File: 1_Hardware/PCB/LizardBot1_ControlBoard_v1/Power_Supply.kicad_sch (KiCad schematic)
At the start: 49 parts, among them J201 Conn_01x02, J202 Screw_Terminal_01x02, J203 Conn_01x02, J204 Conn_01x02, J205 Conn_01x02, Q201 SQ4425EY, Q202 AO3401A, SW201 SW_SPST, SW202 SW_Push, U202 AP2112K-3.3

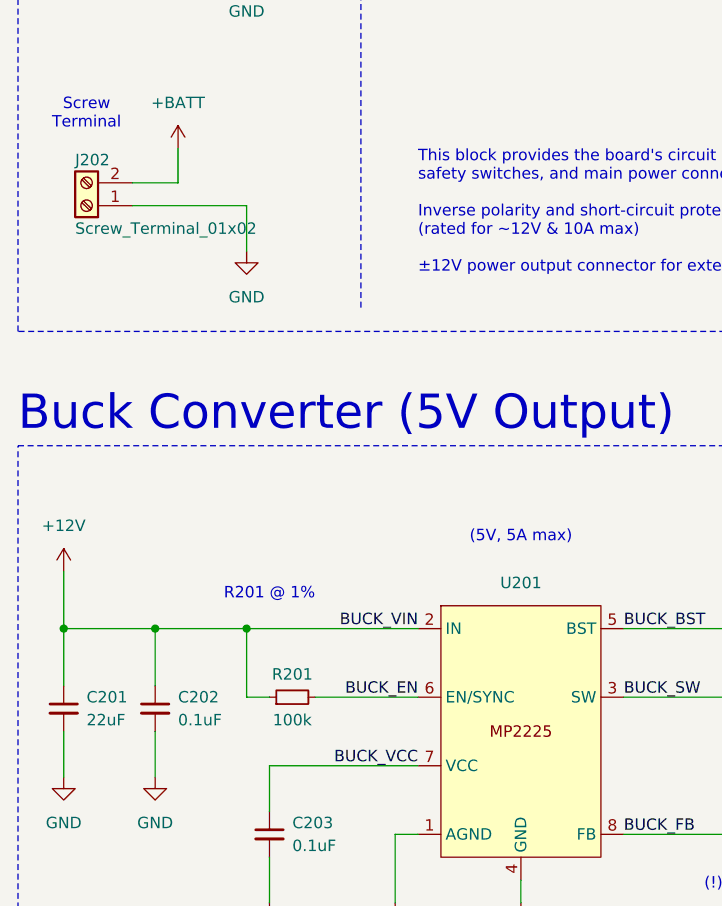
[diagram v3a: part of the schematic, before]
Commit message: Added Peripherals schematic
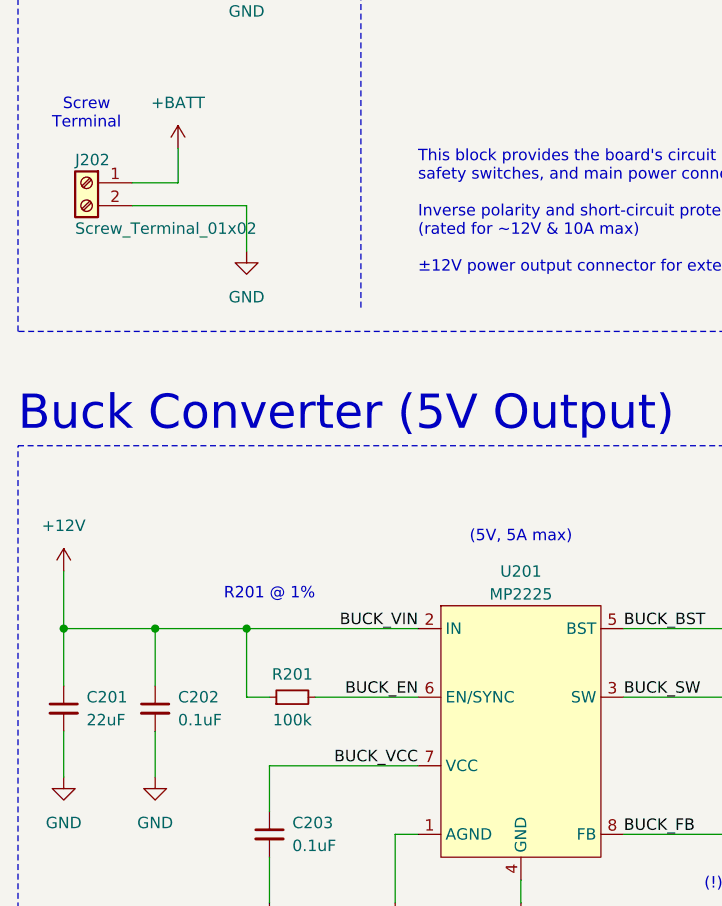
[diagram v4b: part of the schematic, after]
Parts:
- U201: value ~ -> MP2225
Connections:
- net +BATT: now also J202.1 (Pin_1); no longer J202.2 (Pin_2)
- net GND: now also J202.2 (Pin_2); no longer J202.1 (Pin_1)
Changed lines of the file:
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@@
+	)
+	(symbol
+		(lib_id "Connector:Screw_Terminal_01x02")
+		(at 26.67 77.47 0)
+		(mirror y)
+		(unit 1)
+		(exclude_from_sim no)
+		(in_bom yes)
+		(on_board yes)
+		(dnp no)
+		(property "Reference" "J202"
+			(at 25.4 74.93 0)
+			(effects
+				(font
+					(size 1.27 1.27)
+				)
+				(justify right)
+			)
+		)
+		(property "Value" "Screw_Terminal_01x02"
+			(at 25.4 82.55 0)
+			(effects
+				(font
+					(size 1.27 1.27)
+				)
+				(justify right)
+			)
+		)
+		(property "Footprint" ""
+			(at 26.67 77.47 0)
+			(effects
+				(font
+					(size 1.27 1.27)
+				)
+				(hide yes)
+			)
+		)
+		(property "Datasheet" "~"
+			(at 26.67 77.47 0)
+			(effects
+				(font
+					(size 1.27 1.27)
+				)
+				(hide yes)
+			)
+		)
+		(property "Description" "Generic screw terminal, single row, 01x02, script generated (kicad-library-utils/schlib/autogen/connector/)"
+			(at 26.67 77.47 0)
+			(effects
+				(font
+					(size 1.27 1.27)
+				)
+				(hide yes)
+			)
+		)
+		(pin "1"
+		)
+		(pin "2"
+		)
+		(instances
+			(project "LizardBot1_ControlBoard_v1"
+				(path "/1a674a4d-d877-4d7a-ad57-e0a054705c31/1ad8e535-9964-46ac-bb04-941393eb127d"
+					(reference "J202")
+					(unit 1)
+				)
+			)
+		)
 	)
 	(symbol
@@
 		(on_board yes)
 		(dnp no)
-		(fields_autoplaced yes)
 		(property "Reference" "U201"
-			(at 74.93 121.92 0)
-			(effects
-				(font
-					(size 1.27 1.27)
-				)
-			)
-		)
-		(property "Value" "~"
-			(at 74.93 138.43 0)
-			(effects
-				(font
-					(size 1.27 1.27)
-				)
-				(hide yes)
+			(at 74.93 120.65 0)
+			(effects
+				(font
+					(size 1.27 1.27)
+				)
+			)
+		)
+		(property "Value" "MP2225"
+			(at 74.93 123.19 0)
+			(effects
+				(font
+					(size 1.27 1.27)
+				)
 			)
 		)
@@
 					(unit 1)
 				)
-			)
-		)
-	)
-	(symbol
-		(lib_id "Connector:Screw_Terminal_01x02")
-		(at 26.67 80.01 180)
-		(unit 1)
-		(exclude_from_sim no)
-		(in_bom yes)
-		(on_board yes)
-		(dnp no)
-		(property "Reference" "J202"
-			(at 25.4 74.93 0)
-			(effects
-				(font
-					(size 1.27 1.27)
-				)
-				(justify right)
-			)
-		)
-		(property "Value" "Screw_Terminal_01x02"
-			(at 25.4 82.55 0)
-			(effects
-				(font
-					(size 1.27 1.27)
-				)
-				(justify right)
-			)
-		)
-		(property "Footprint" ""
-			(at 26.67 80.01 0)
-			(effects
-				(font
-					(size 1.27 1.27)
-				)
-				(hide yes)
-			)
-		)
-		(property "Datasheet" "~"
-			(at 26.67 80.01 0)
-			(effects
-				(font
-					(size 1.27 1.27)
-				)
-				(hide yes)
-			)
-		)
-		(property "Description" "Generic screw terminal, single row, 01x02, script generated (kicad-library-utils/schlib/autogen/connector/)"
-			(at 26.67 80.01 0)
-			(effects
-				(font
-					(size 1.27 1.27)
-				)
-				(hide yes)
-			)
-		)
-		(pin "1"
-		)
-		(pin "2"
-		)
-		(instances
-			(project ""
-				(path "/1a674a4d-d877-4d7a-ad57-e0a054705c31/1ad8e535-9964-46ac-bb04-941393eb127d"
-					(reference "J202")
-					(unit 1)
-				)

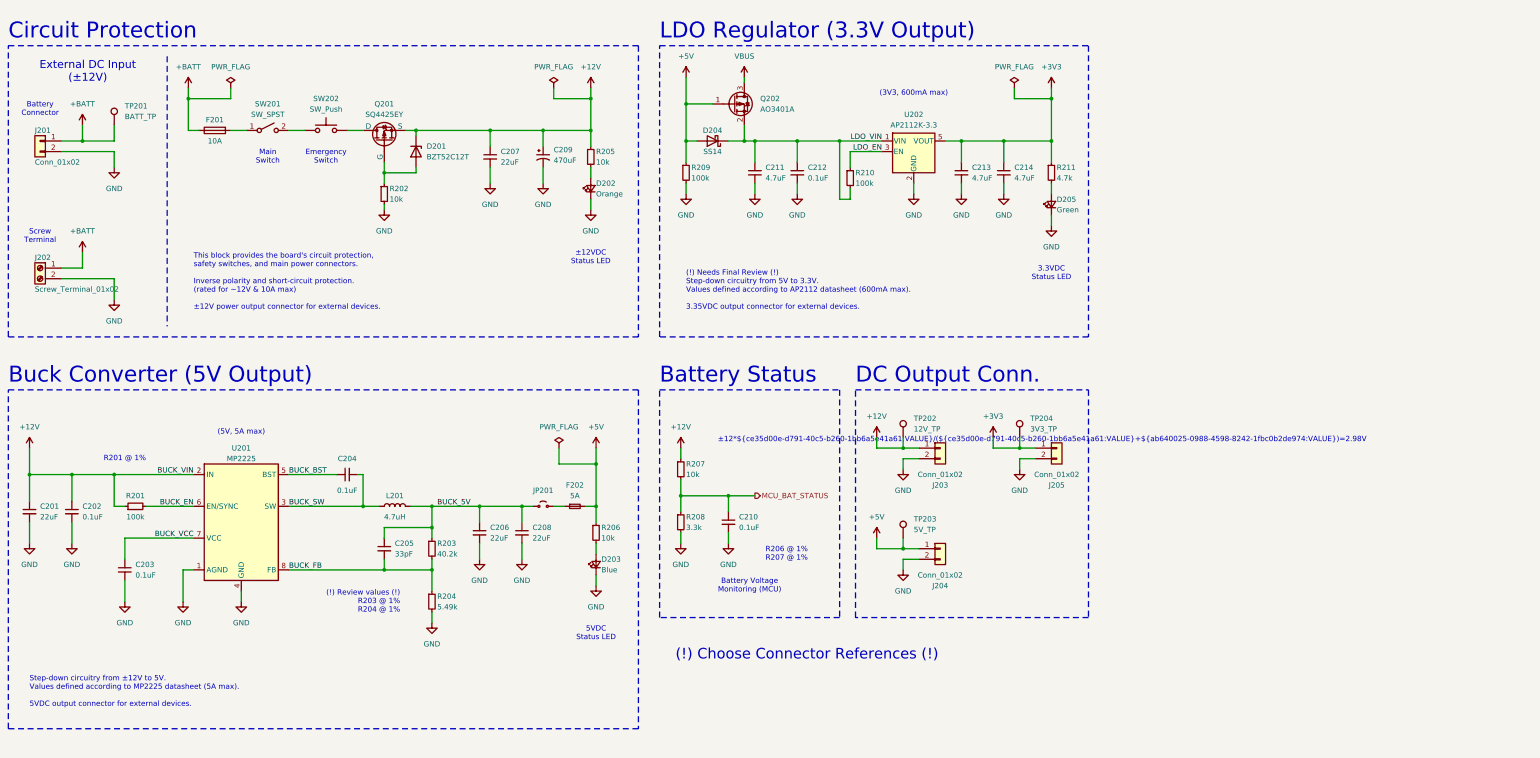
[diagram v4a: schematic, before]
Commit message: Added Communication_Interfaces schematic
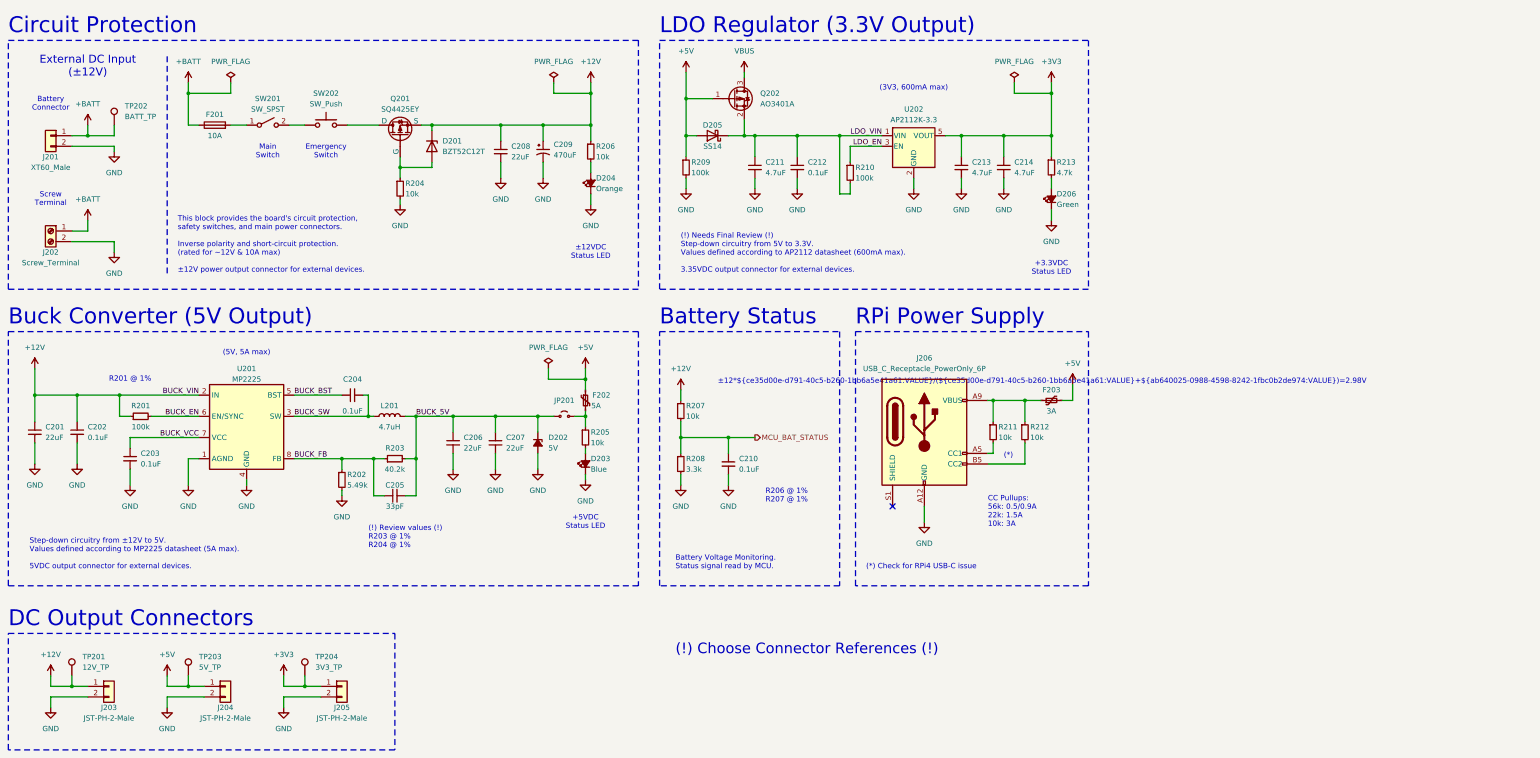
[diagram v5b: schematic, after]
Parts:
- removed D202: Orange, symbol Device:LED_Small
- removed D203: Blue, symbol Device:LED_Small
- removed D205: Green, symbol Device:LED_Small
- removed F202: 5A, symbol Device:Fuse_Small
- added D202: 5V, symbol Device:D_Zener_Small_Filled
- added D203: Blue, symbol Device:LED_Small_Filled
- added D204: Orange, symbol Device:LED_Small_Filled
- added D206: Green, symbol Device:LED_Small_Filled
- added F202: 5A, symbol Device:Polyfuse_Small
- added F203: 3A, symbol Device:Polyfuse_Small
- added J206: USB_C_Receptacle_PowerOnly_6P, symbol Connector:USB_C_Receptacle_PowerOnly_6P
- added R211, R212: 10k, symbol Device:R_Small
- J201: value Conn_01x02 -> XT60_Male
- J202: value Screw_Terminal_01x02 -> Screw_Terminal
- J203, J204, J205: value Conn_01x02 -> JST-PH-2-Male
- renumbered C208 to C207, C207 to C208, D204 to D205, R204 to R202, R202 to R204, R206 to R205, R205 to R206, R211 to R213, TP202 to TP201, TP201 to TP202
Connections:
- net +5V: now also F202.1, F203.2; no longer R205.1
- net BUCK_5V: now also C205.2, R203.2, D202.1 (K); no longer C205.1, R203.1
- net BUCK_FB: now also C205.1, R203.1; no longer C205.2, R203.2
- net GND: now also D202.2 (A), D203.1 (K), D204.1 (K), D206.1 (K), J206.A12 (GND), J206.B12 (GND)
- net at R213.2: now also D206.2 (A)
- net at JP201.2 (B): now also R205.1, F202.2
- net at R205.2: now also D203.2 (A)
- net at R206.2: now also D204.2 (A)
- new net: J206.A5 (CC1), R211.2
- new net: F203.1, J206.A9 (VBUS), J206.B9 (VBUS), R211.1, R212.1
- new net: J206.B5 (CC2), R212.2
- no-connect marks 0 -> 1
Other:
- note added: "(*)"
- note added: "(*) Check for RPi4 USB-C issue"
- note added: "+3.3VDC Status LED"
- note added: "+5VDC Status LED"
- note added: "Battery Voltage Monitoring. Status signal read by MCU."
- note added: "CC Pullups: 56k: 0.5/0.9A 22k: 1.5A 10k: 3A"
- note added: "DC Output Connectors"
- note added: "RPi Power Supply"
- note removed: "3.3VDC Status LED"
- note removed: "5VDC Status LED"
- note removed: "Battery Voltage Monitoring (MCU)"
- note removed: "DC Output Conn."
- moved on the sheet: C201, C202, C203, C204, C206, C207, C208, C209, C210, C211, C212, C213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

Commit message: PCB schematics revision
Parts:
- removed D202: 5V, symbol Device:D_Zener_Small_Filled
- removed D205: SS14, symbol Device:D_Schottky
- removed Q202: AO3401A, Package_TO_SOT_SMD:SOT-23, symbol Transistor_FET:AO3401A
- removed R209: 100k, symbol Device:R_Small
- removed TP201: 12V_TP, symbol Connector:TestPoint
- removed TP202: BATT_TP, symbol Connector:TestPoint
- removed TP203: 5V_TP, symbol Connector:TestPoint
- removed TP204: 3V3_TP, symbol Connector:TestPoint
- added D204: SS1P3L, symbol Device:D_Schottky_Small_Filled
- added SW203: SW_SPDT, symbol Switch:SW_SPDT
- J201: value XT60_Male -> XT60-M
- J202: value Screw_Terminal -> Receptable-5.08-2P
- renumbered D203 to D202, D204 to D203, D206 to D205, R210 to R209, R211 to R210, R212 to R211, R213 to R212
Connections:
- net +5V: now also JP201.2 (B), R205.1, SW203.1 (A); no longer F202.1
- net BUCK_5V: now also F202.1; no longer JP201.1 (A)
- net LDO_VIN: now also SW203.2 (B)
- net VBUS: now also D204.2 (A)
- new net: F202.2, JP201.1 (A)
- new net: D204.1 (K), SW203.3 (C)
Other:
- note added: "(!) Needs Final Review (!) Step-down circuitry from 5V to 3.3V. Values defined according to AP2112 datasheet (600mA max)."
- note added: "CC Host Pullups: 56k: 0.5/0.9A 22k: 1.5A 10k: 3A"
- note added: "Step-down circuitry from ±12V to 5V. Values defined according to MP2225 datasheet (5A max)."
- note added: "Terminal Block"
- note added: "This block provides the board's circuit protection, safety switches, and main power connectors. Inverse polarity and short-circuit protection. (rated for ~12V & 10A max)"
- note removed: "(!) Choose Connector References (!)"
- note removed: "(!) Needs Final Review (!) Step-down circuitry from 5V to 3.3V. Values defined according to AP2112 datasheet (600mA max). 3.35VDC output connector for external devices."
- note removed: "CC Pullups: 56k: 0.5/0.9A 22k: 1.5A 10k: 3A"
- note removed: "Screw Terminal"
- note removed: "Step-down circuitry from ±12V to 5V. Values defined according to MP2225 datasheet (5A max). 5VDC output connector for external devices."
- note removed: "This block provides the board's circuit protection, safety switches, and main power connectors. Inverse polarity and short-circuit protection. (rated for ~12V & 10A max) ±12V power output connector for external devices."
- moved on the sheet: C201, C202, C203, C204, C205, C206, C207, C208, C209, C211, C212, C213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
